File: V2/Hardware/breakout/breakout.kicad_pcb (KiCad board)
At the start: 2 copper layers, 8 parts, among them J0 Flat_7seg_F, J1 Conn_D, J2 Conn_C, J3 Conn_E, J4 Conn_B, J5 Conn_F, J6 Conn_A, J7 Conn_G

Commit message: revision 2 boards
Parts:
- added Screw: MountingHole_3.2mm_M3, MountingHole:MountingHole_3.2mm_M3, F.Cu at (190.0, 86.0)
- added Screw: MountingHole_3.2mm_M3, MountingHole:MountingHole_3.2mm_M3, F.Cu at (190.0, 61.0)
- added Screw: MountingHole_3.2mm_M3, MountingHole:MountingHole_3.2mm_M3, F.Cu at (127.0, 86.0)
- added Screw: MountingHole_3.2mm_M3, MountingHole:MountingHole_3.2mm_M3, F.Cu at (127.0, 61.0)
- J0: value Flat_7seg_F -> 7SEG_12V; footprint Connector_PinHeader_2.54mm:PinHeader_2x05_P2.54mm_Horizontal -> Connector_IDC:IDC-Header_2x05-1MP_P2.54mm_Latch_Vertical
- J1, J2, J3, J4, J5, J6, J7: footprint Connector_PinSocket_2.54mm:PinSocket_1x02_P2.54mm_Vertical -> Connector_Molex:Molex_KK-254_AE-6410-02A_1x02_P2.54mm_Vertical
- moved J0 2.00 mm to (163.0, 76.0)
- moved J3 1.00 mm to (151.0, 62.0), turned to 180 degrees
- moved J5 1.00 mm to (143.0, 62.0), turned to 180 degrees
- moved J6 0.54 mm to (183.5, 62.0), turned to 180 degrees
- moved J1 0.46 mm to (159.5, 62.0), turned to 180 degrees
- moved J2 0.46 mm to (167.5, 62.0), turned to 180 degrees
- moved J4 0.46 mm to (175.5, 62.0), turned to 180 degrees
- moved J7 0.46 mm to (135.5, 62.0), turned to 180 degrees
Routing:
- net /SEG_A: track 41.7 -> 62.9 mm
- net /SEG_B: track 29.6 -> 47.5 mm
- net /+12V: track 180.8 -> 194.5 mm
- net /SEG_C: track 18.6 -> 22.8 mm
- net (no net): track 4.00 -> 0.00 mm, vias 4 -> 0
- net /SEG_F: track 24.1 -> 27.3 mm
- net /SEG_G: track 28.1 -> 29.9 mm
- net /SEG_E: track 20.7 -> 22.1 mm
- net /SEG_D: track 16.1 -> 16.9 mm
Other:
- board text added: "33 mm"
- board text added: "71 mm"
- board text removed: "33mm"
- board text removed: "56mm"

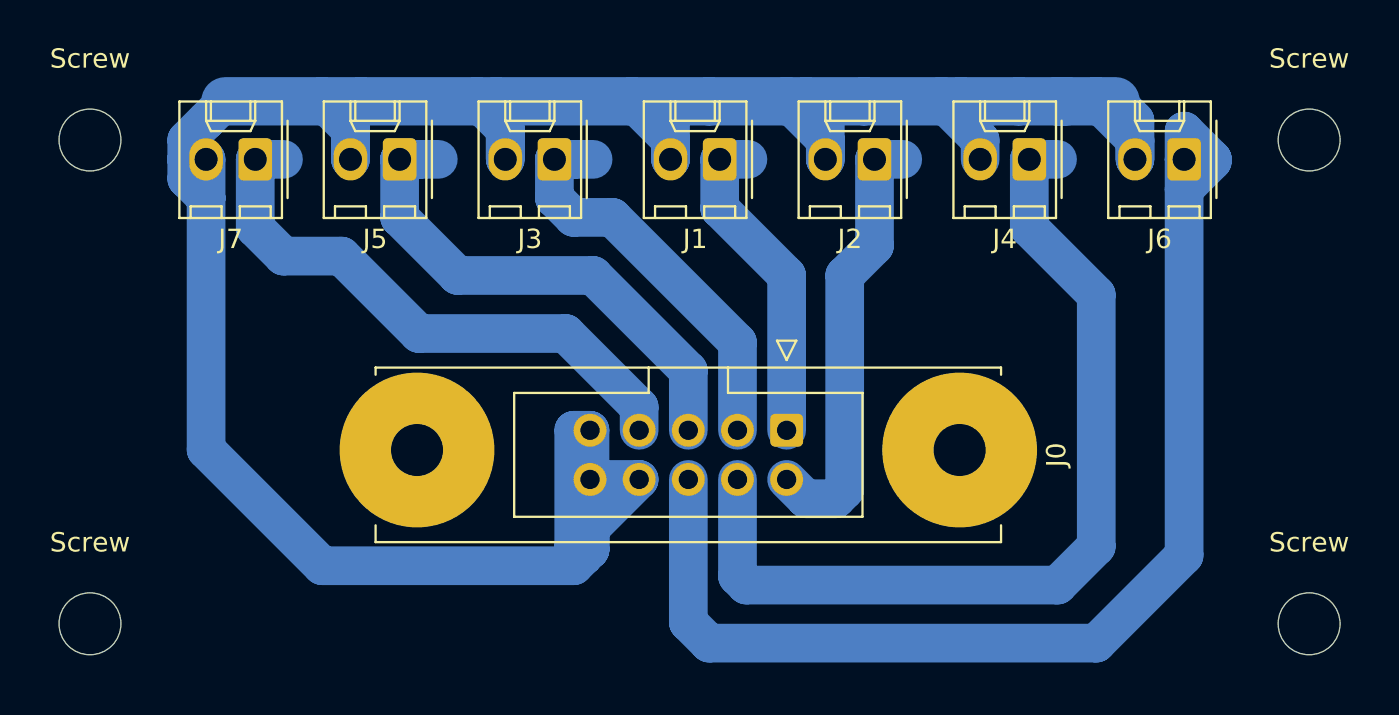
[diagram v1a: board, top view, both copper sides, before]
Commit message: Remove version 1 board
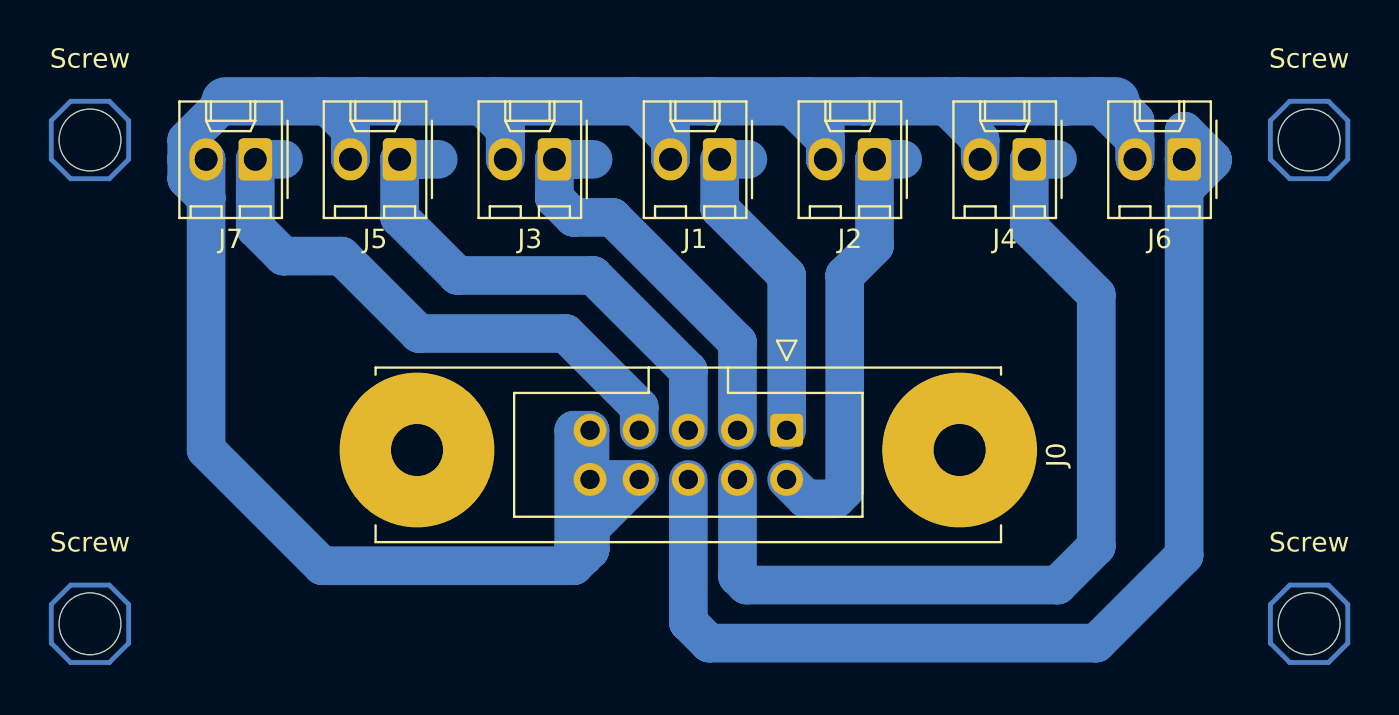
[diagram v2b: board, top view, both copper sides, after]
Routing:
- net (no net): track 0.00 -> 54.6 mm, vias 0 -> 4
